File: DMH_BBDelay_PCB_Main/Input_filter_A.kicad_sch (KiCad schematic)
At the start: 16 parts, among them U21 TL072

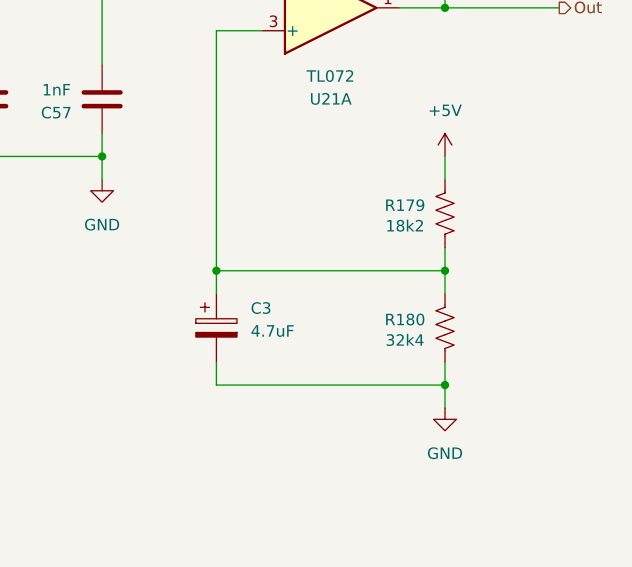
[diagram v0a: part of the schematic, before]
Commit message: Changed input filter position in the signal chain
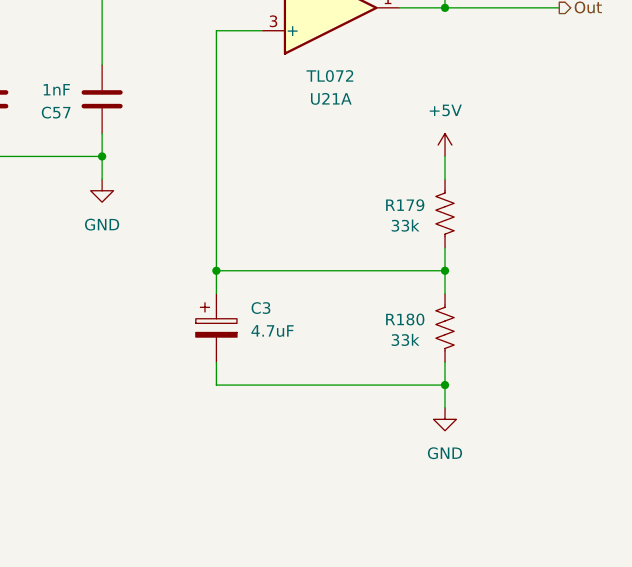
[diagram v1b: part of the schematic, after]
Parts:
- R179: value 18k2 -> 33k
- R180: value 32k4 -> 33k
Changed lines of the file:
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@@
 			)
 		)
-		(property "Value" "18k2"
+		(property "Value" "33k"
 			(at 135.255 90.297 0)
 			(show_name no)
@@
 			)
 		)
-		(property "Value" "32k4"
+		(property "Value" "33k"
 			(at 135.255 102.997 0)
 			(show_name no)

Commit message: Moved input filter again
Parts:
- removed C3: 4.7uF, Capacitor_THT:CP_Radial_D5.0mm_P2.00mm, symbol Device:C_Polarized
- removed R179, R180: 33k, Resistor_THT:R_Axial_DIN0207_L6.3mm_D2.5mm_P7.62mm_Horizontal, symbol Device:R_US
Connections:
- net GND: now also U21.3 (+)

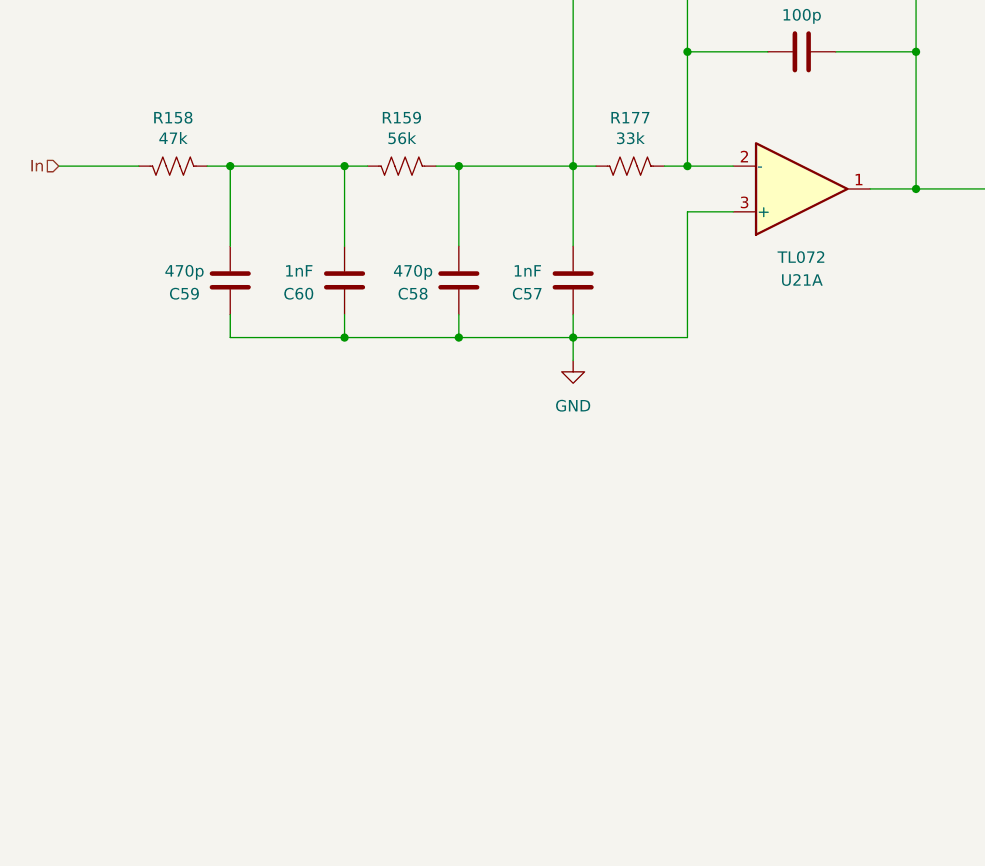
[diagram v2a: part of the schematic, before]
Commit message: Inserted compander in Channel A path
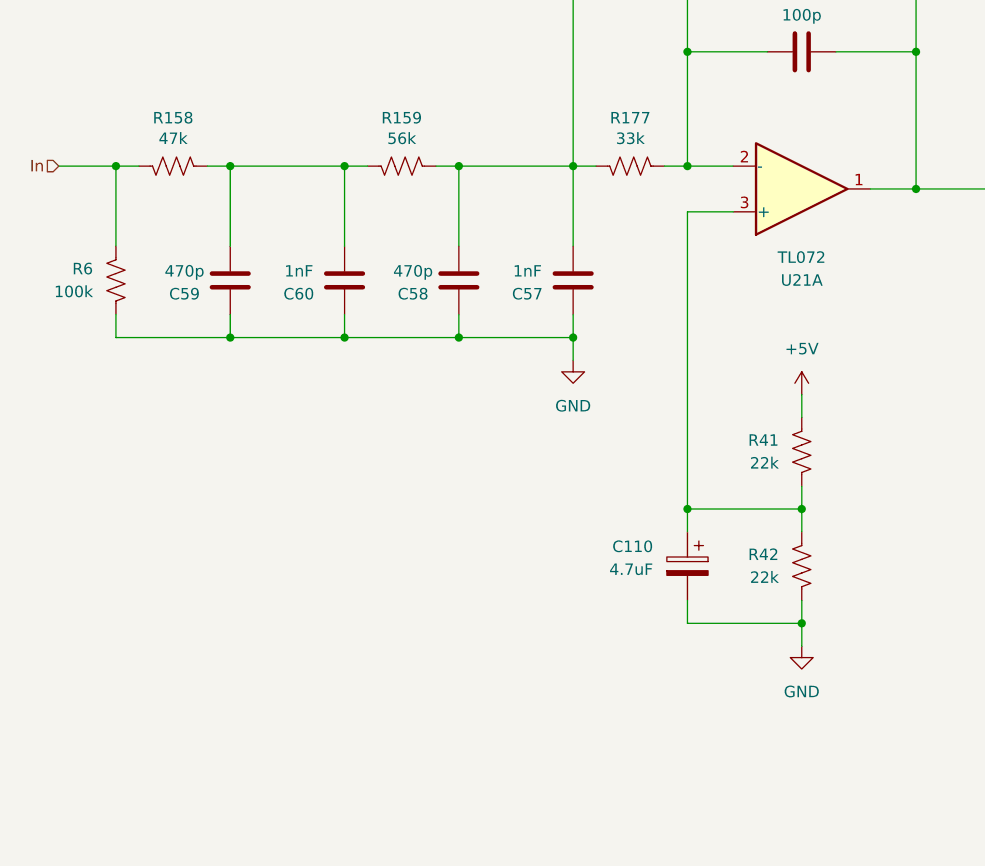
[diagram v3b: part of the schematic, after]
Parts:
- added C110: 4.7uF, Capacitor_THT:CP_Radial_D4.0mm_P1.50mm, symbol Device:C_Polarized
- added R41, R42: 22k, Resistor_THT:R_Axial_DIN0207_L6.3mm_D2.5mm_P7.62mm_Horizontal, symbol Device:R_US
- added R6: 100k, Resistor_THT:R_Axial_DIN0207_L6.3mm_D2.5mm_P7.62mm_Horizontal, symbol Device:R_US
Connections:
- net GND: now also C110.2, R42.1, R6.1; no longer U21.3 (+)
- net In: now also R6.2
- new net: C110.1, R41.1, R42.2, U21.3 (+)
- new net +5V: R41.2

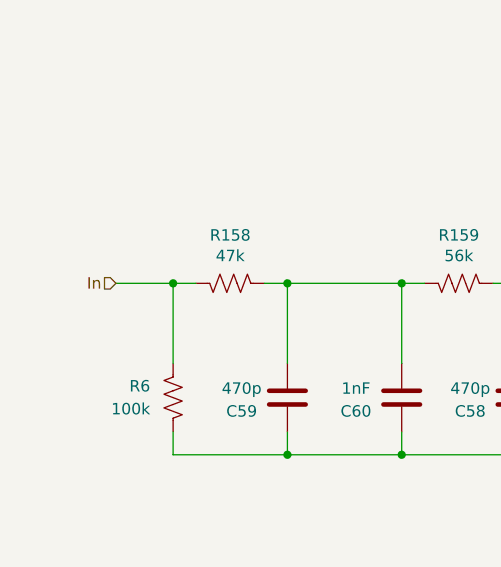
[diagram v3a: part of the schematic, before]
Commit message: Inserted compander into channel B path
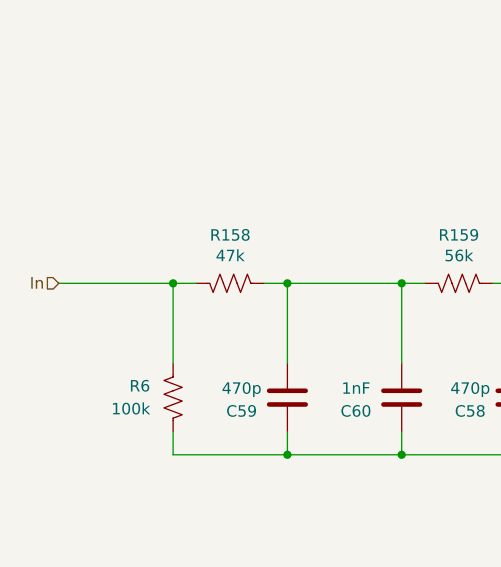
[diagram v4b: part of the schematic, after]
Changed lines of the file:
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@@
+	)
+	(junction
+		(at 139.7 166.37)
+		(diameter 0)
+		(color 0 0 0 0)
+	)
+	(junction
+		(at 63.5 82.55)
+		(diameter 0)
+		(color 0 0 0 0)
+	)
+	(junction
+		(at 114.3 63.5)
+		(diameter 0)
+		(color 0 0 0 0)
+	)
+	(junction
+		(at 76.2 82.55)
+		(diameter 0)
+		(color 0 0 0 0)
+	)
+	(junction
+		(at 63.5 63.5)
+		(diameter 0)
+		(color 0 0 0 0)
+	)
+	(junction
+		(at 76.2 63.5)
+		(diameter 0)
+		(color 0 0 0 0)
+	)
+	(junction
+		(at 114.3 101.6)
+		(diameter 0)
+		(color 0 0 0 0)
+	)
+	(junction
+		(at 127 177.8)
+		(diameter 0)
+		(color 0 0 0 0)
+	)
+	(junction
+		(at 127 154.94)
+		(diameter 0)
+		(color 0 0 0 0)
+	)
+	(junction
+		(at 88.9 82.55)
+		(diameter 0)
+		(color 0 0 0 0)
+	)
+	(junction
+		(at 101.6 82.55)
+		(diameter 0)
+		(color 0 0 0 0)
+	)
+	(junction
+		(at 139.7 50.8)
+		(diameter 0)
+		(color 0 0 0 0)
+	)
+	(junction
+		(at 101.6 63.5)
+		(diameter 0)
+		(color 0 0 0 0)
 	)
 	(junction
@@
 	)
 	(junction
-		(at 139.7 166.37)
-		(diameter 0)
-		(color 0 0 0 0)
-	)
-	(junction
-		(at 63.5 82.55)
-		(diameter 0)
-		(color 0 0 0 0)
-	)
-	(junction
-		(at 114.3 63.5)
-		(diameter 0)
-		(color 0 0 0 0)
-	)
-	(junction
-		(at 76.2 82.55)
-		(diameter 0)
-		(color 0 0 0 0)
-	)
-	(junction
-		(at 63.5 63.5)
-		(diameter 0)
-		(color 0 0 0 0)
-	)
-	(junction
-		(at 76.2 63.5)
-		(diameter 0)
-		(color 0 0 0 0)
-	)
-	(junction
-		(at 114.3 101.6)
-		(diameter 0)
-		(color 0 0 0 0)
-	)
-	(junction
-		(at 127 177.8)
-		(diameter 0)
-		(color 0 0 0 0)
-	)
-	(junction
-		(at 127 154.94)
-		(diameter 0)
-		(color 0 0 0 0)
-	)
-	(junction
-		(at 88.9 82.55)
-		(diameter 0)
-		(color 0 0 0 0)
-	)
-	(junction
-		(at 101.6 82.55)
-		(diameter 0)
-		(color 0 0 0 0)
-	)
-	(junction
-		(at 139.7 50.8)
-		(diameter 0)
-		(color 0 0 0 0)
-	)
-	(junction
-		(at 101.6 63.5)
-		(diameter 0)
-		(color 0 0 0 0)
-	)
-	(junction
 		(at 127 101.6)
 		(diameter 0)
@@
 	(wire
 		(pts
-			(xy 44.45 63.5) (xy 50.8 63.5)
+			(xy 38.1 63.5) (xy 50.8 63.5)
 		)
 		(stroke
@@
 	(hierarchical_label "In"
 		(shape input)
-		(at 44.45 63.5 180)
+		(at 38.1 63.5 180)
 		(effects
 			(font

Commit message: Adjustments during breadboarding
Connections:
- net Ref_2v5: now reaches C110.1, R41.1, R42.2, U21.3 (+)
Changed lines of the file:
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@@
+	(wire
+		(pts
+			(xy 127 101.6) (xy 133.35 101.6)
+		)
+		(stroke
+			(width 0)
+			(type default)
+		)
+	)
 	(wire
 		(pts
@@
 		)
 	)
+	(global_label "Ref_2v5"
+		(shape output)
+		(at 133.35 101.6 0)
+		(fields_autoplaced yes)
+		(effects
+			(font
+				(size 1.27 1.27)
+			)
+			(justify left)
+		)
+		(property "Intersheetrefs" "${INTERSHEET_REFS}"
+			(at 143.7737 101.6 0)
+			(hide yes)
+			(show_name no)
+			(do_not_autoplace no)
+			(effects
+				(font
+					(size 1.27 1.27)
+				)
+				(justify left)
+			)
+		)
+	)

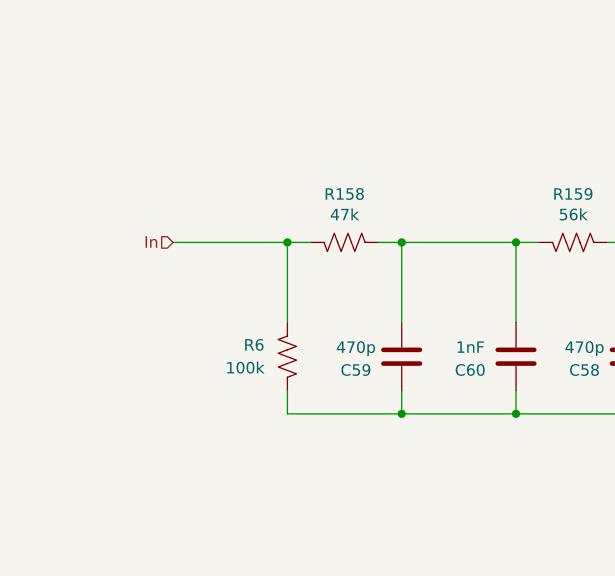
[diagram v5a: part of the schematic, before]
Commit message: More adjustments during breadboarding
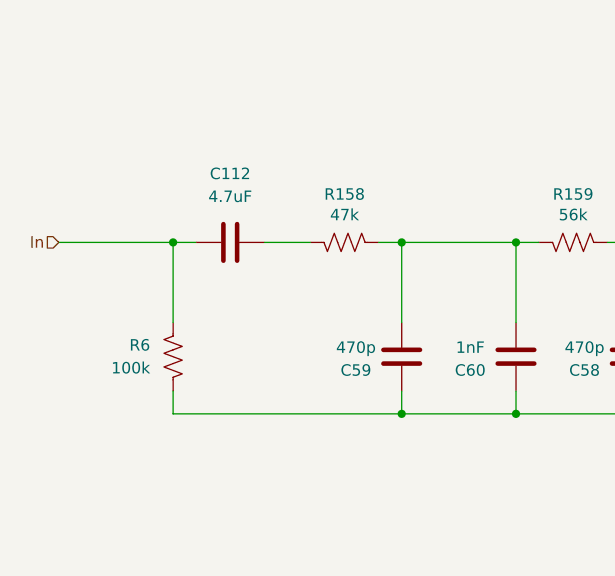
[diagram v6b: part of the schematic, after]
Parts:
- added C112: 4.7uF, Capacitor_THT:C_Disc_D4.3mm_W1.9mm_P5.00mm, symbol Device:C
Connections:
- net In: now also C112.1; no longer R158.1
- new net: C112.2, R158.1
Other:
- moved on the sheet: R6
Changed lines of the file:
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@@
+	)
+	(junction
+		(at 63.5 82.55)
+		(diameter 0)
+		(color 0 0 0 0)
 	)
 	(junction
@@
 	)
 	(junction
-		(at 63.5 82.55)
-		(diameter 0)
-		(color 0 0 0 0)
-	)
-	(junction
 		(at 114.3 63.5)
 		(diameter 0)
@@
 	)
 	(junction
-		(at 50.8 63.5)
+		(at 38.1 63.5)
 		(diameter 0)
 		(color 0 0 0 0)
@@
 	(wire
 		(pts
-			(xy 50.8 63.5) (xy 53.34 63.5)
+			(xy 38.1 63.5) (xy 40.64 63.5)
 		)
 		(stroke
@@
 	(wire
 		(pts
-			(xy 50.8 80.01) (xy 50.8 82.55)
+			(xy 38.1 80.01) (xy 38.1 82.55)
 		)
 		(stroke
@@
 	(wire
 		(pts
+			(xy 48.26 63.5) (xy 53.34 63.5)
+		)
+		(stroke
+			(width 0)
+			(type default)
+		)
+	)
+	(wire
+		(pts
 			(xy 139.7 166.37) (xy 139.7 168.91)
 		)
@@
 	(wire
 		(pts
-			(xy 50.8 82.55) (xy 63.5 82.55)
+			(xy 38.1 82.55) (xy 63.5 82.55)
 		)
 		(stroke
@@
 	(wire
 		(pts
-			(xy 38.1 63.5) (xy 50.8 63.5)
+			(xy 25.4 63.5) (xy 38.1 63.5)
 		)
 		(stroke
@@
 	(wire
 		(pts
-			(xy 50.8 63.5) (xy 50.8 72.39)
+			(xy 38.1 63.5) (xy 38.1 72.39)
 		)
 		(stroke
@@
 	(hierarchical_label "In"
 		(shape input)
-		(at 38.1 63.5 180)
+		(at 25.4 63.5 180)
 		(effects
 			(font
@@
 	)
 	(symbol
+		(lib_id "Device:C")
+		(at 44.45 63.5 90)
+		(unit 1)
+		(body_style 1)
+		(exclude_from_sim no)
+		(in_bom yes)
+		(on_board yes)
+		(in_pos_files yes)
+		(dnp no)
+		(fields_autoplaced yes)
+		(property "Reference" "C112"
+			(at 44.45 55.88 90)
+			(show_name no)
+			(do_not_autoplace no)
+			(effects
+				(font
+					(size 1.27 1.27)
+				)
+			)
+		)
+		(property "Value" "4.7uF"
+			(at 44.45 58.42 90)
+			(show_name no)
+			(do_not_autoplace no)
+			(effects
+				(font
+					(size 1.27 1.27)
+				)
+			)
+		)
+		(property "Footprint" "Capacitor_THT:C_Disc_D4.3mm_W1.9mm_P5.00mm"
+			(at 48.26 62.5348 0)
+			(hide yes)
+			(show_name no)
+			(do_not_autoplace no)
+			(effects
+				(font
+					(size 1.27 1.27)
+				)
+			)
+		)
+		(property "Datasheet" ""
+			(at 44.45 63.5 0)
+			(hide yes)
+			(show_name no)
+			(do_not_autoplace no)
+			(effects
+				(font
+					(size 1.27 1.27)
+				)
+			)
+		)
+		(property "Description" "Unpolarized capacitor"
+			(at 44.45 63.5 0)
+			(hide yes)
+			(show_name no)
+			(do_not_autoplace no)
+			(effects
+				(font
+					(size 1.27 1.27)
+				)
+			)
+		)
+		(pin "1"
+		)
+		(pin "2"
+		)
+		(instances
+			(project "DMH_BBDelay_PCB_Main"
+				(path "/58f4306d-5387-4983-bb08-41a2313fd315/7ad2d702-dfb7-4d49-a82d-34430dd5948f/7229ae76-44f4-4595-8819-8d092fe99e78"
+					(reference "C112")
+					(unit 1)
+				)
+			)
+		)
+	)
+	(symbol
 		(lib_id "Device:R_US")
 		(at 107.95 63.5 90)
@@
 	(symbol
 		(lib_id "Device:R_US")
-		(at 50.8 76.2 0)
+		(at 38.1 76.2 0)
 		(mirror x)
 		(unit 1)
@@
 		(dnp no)
 		(property "Reference" "R6"
-			(at 48.26 74.9299 0)
+			(at 35.56 74.9299 0)
 			(show_name no)
 			(do_not_autoplace no)
@@
 		)
 		(property "Value" "100k"
-			(at 48.26 77.4699 0)
+			(at 35.56 77.4699 0)
 			(show_name no)
 			(do_not_autoplace no)
@@
 		)
 		(property "Footprint" "Resistor_THT:R_Axial_DIN0207_L6.3mm_D2.5mm_P7.62mm_Horizontal"
-			(at 51.816 75.946 90)
+			(at 39.116 75.946 90)
 			(hide yes)
 			(show_name no)
@@
 		)
 		(property "Datasheet" ""
-			(at 50.8 76.2 0)
+			(at 38.1 76.2 0)
 			(hide yes)
 			(show_name no)
@@
 		)
 		(property "Description" "Resistor, US symbol"
-			(at 50.8 76.2 0)
-			(hide yes)
-			(show_name no)
+			(at 38.1 76.2 0)
+			(hide yes)
+			(show_name no)

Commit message: Added notes from troubleshooting
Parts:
- C112: value 4.7uF -> 3.3uF
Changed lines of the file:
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@@
 			)
 		)
-		(property "Value" "4.7uF"
+		(property "Value" "3.3uF"
 			(at 44.45 58.42 90)
 			(show_name no)
